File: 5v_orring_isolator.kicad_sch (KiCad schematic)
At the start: 11 parts, among them IC2 NPS4053GVH, U4 TBA2-2411, U6 TPS2116DRL

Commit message: footprint assignment again
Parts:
- C20: renamed from C19; footprint (none) -> Capacitor_SMD:C_0805_2012Metric
- C21: footprint (none) -> Capacitor_SMD:C_0805_2012Metric
- C22: renamed from C20; footprint (none) -> Capacitor_SMD:C_0805_2012Metric
- IC2: footprint SOT95P275X110-6N -> UTSVT_Power:SOT95P275X110-6N
- R36, R37: footprint (none) -> Resistor_SMD:R_0805_2012Metric
- renumbered R28 to R33, R29 to R34, R30 to R35, U6 to U5, U4 to U6
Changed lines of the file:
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@@
 		(dnp no)
 		(fields_autoplaced yes)
-		(property "Reference" "#PWR050"
+		(property "Reference" "#PWR060"
 			(at 39.37 121.92 0)
 			(effects
@@
 			(project "USBCPowerPCB"
 				(path "/f58400c5-df4b-4929-8d2b-33c0fe23fcd9/3390d9c6-6b88-417e-a6aa-b25c6fe8fa66"
-					(reference "#PWR050")
+					(reference "#PWR060")
 					(unit 1)
 				)
@@
 		(dnp no)
 		(fields_autoplaced yes)
-		(property "Reference" "U4"
+		(property "Reference" "U6"
 			(at 147.32 95.25 0)
 			(effects
@@
 			(project ""
 				(path "/f58400c5-df4b-4929-8d2b-33c0fe23fcd9/3390d9c6-6b88-417e-a6aa-b25c6fe8fa66"
-					(reference "U4")
+					(reference "U6")
 					(unit 1)
 				)
@@
 		(dnp no)
 		(fields_autoplaced yes)
-		(property "Reference" "#PWR035"
+		(property "Reference" "#PWR061"
 			(at 85.09 121.92 0)
 			(effects
@@
 			(project "USBCPowerPCB"
 				(path "/f58400c5-df4b-4929-8d2b-33c0fe23fcd9/3390d9c6-6b88-417e-a6aa-b25c6fe8fa66"
-					(reference "#PWR035")
+					(reference "#PWR061")
 					(unit 1)
 				)
@@
 		(on_board yes)
 		(dnp no)
-		(property "Reference" "#PWR067"
+		(property "Reference" "#PWR064"
 			(at 194.31 111.76 0)
 			(effects
@@
 			(project "USBCPowerPCB"
 				(path "/f58400c5-df4b-4929-8d2b-33c0fe23fcd9/3390d9c6-6b88-417e-a6aa-b25c6fe8fa66"
-					(reference "#PWR067")
+					(reference "#PWR064")
 					(unit 1)
 				)
@@
 		(dnp no)
 		(fields_autoplaced yes)
-		(property "Reference" "R28"
+		(property "Reference" "R33"
 			(at 41.91 99.0599 0)
 			(effects
@@
 			(project "USBCPowerPCB"
 				(path "/f58400c5-df4b-4929-8d2b-33c0fe23fcd9/3390d9c6-6b88-417e-a6aa-b25c6fe8fa66"
-					(reference "R28")
+					(reference "R33")
 					(unit 1)
 				)
@@
 		(on_board yes)
 		(dnp no)
-		(property "Reference" "#PWR043"
+		(property "Reference" "#PWR063"
 			(at 158.75 114.3 0)
 			(effects
@@
 			(project "USBCPowerPCB"
 				(path "/f58400c5-df4b-4929-8d2b-33c0fe23fcd9/3390d9c6-6b88-417e-a6aa-b25c6fe8fa66"
-					(reference "#PWR043")
+					(reference "#PWR063")
 					(unit 1)
 				)
@@
 		(on_board yes)
 		(dnp no)
-		(property "Reference" "#PWR042"
+		(property "Reference" "#PWR062"
 			(at 135.89 115.57 0)
 			(effects
@@
 			(project "USBCPowerPCB"
 				(path "/f58400c5-df4b-4929-8d2b-33c0fe23fcd9/3390d9c6-6b88-417e-a6aa-b25c6fe8fa66"
-					(reference "#PWR042")
+					(reference "#PWR062")
 					(unit 1)
 				)
@@
 		(dnp no)
 		(fields_autoplaced yes)
-		(property "Reference" "U6"
+		(property "Reference" "U5"
 			(at 85.09 91.44 0)
 			(effects
@@
 			(project "USBCPowerPCB"
 				(path "/f58400c5-df4b-4929-8d2b-33c0fe23fcd9/3390d9c6-6b88-417e-a6aa-b25c6fe8fa66"
-					(reference "U6")
+					(reference "U5")
 					(unit 1)
 				)
@@
 		(dnp no)
 		(fields_autoplaced yes)
-		(property "Reference" "R30"
+		(property "Reference" "R35"
 			(at 99.06 102.8699 0)
 			(effects
@@
 			(project "USBCPowerPCB"
 				(path "/f58400c5-df4b-4929-8d2b-33c0fe23fcd9/3390d9c6-6b88-417e-a6aa-b25c6fe8fa66"
-					(reference "R30")
+					(reference "R35")
 					(unit 1)
 				)
@@
 		(dnp no)
 		(fields_autoplaced yes)
-		(property "Reference" "R29"
+		(property "Reference" "R34"
 			(at 41.91 109.2199 0)
 			(effects
@@
 			(project "USBCPowerPCB"
 				(path "/f58400c5-df4b-4929-8d2b-33c0fe23fcd9/3390d9c6-6b88-417e-a6aa-b25c6fe8fa66"
-					(reference "R29")
+					(reference "R34")
 					(unit 1)
 				)
@@
 		(dnp no)
 		(fields_autoplaced yes)
-		(property "Reference" "#PWR065"
+		(property "Reference" "#PWR068"
 			(at 266.7 111.76 0)
 			(effects
@@
 			(project "USBCPowerPCB"
 				(path "/f58400c5-df4b-4929-8d2b-33c0fe23fcd9/3390d9c6-6b88-417e-a6aa-b25c6fe8fa66"
-					(reference "#PWR065")
+					(reference "#PWR068")
 					(unit 1)
 				)
@@
 		(dnp no)
 		(fields_autoplaced yes)
-		(property "Reference" "#PWR068"
+		(property "Reference" "#PWR067"
 			(at 259.08 115.57 0)
 			(effects
@@
 			(project "USBCPowerPCB"
 				(path "/f58400c5-df4b-4929-8d2b-33c0fe23fcd9/3390d9c6-6b88-417e-a6aa-b25c6fe8fa66"
-					(reference "#PWR068")
+					(reference "#PWR067")
 					(unit 1)
 				)
@@
 		(on_board yes)
 		(dnp no)
-		(property "Reference" "C19"
+		(property "Reference" "C20"
 			(at 191.77 101.6062 0)
 			(effects
@@
 			)
 		)
-		(property "Footprint" ""
+		(property "Footprint" "Capacitor_SMD:C_0805_2012Metric"
 			(at 194.31 102.87 0)
 			(effects
@@
 			(project ""
 				(path "/f58400c5-df4b-4929-8d2b-33c0fe23fcd9/3390d9c6-6b88-417e-a6aa-b25c6fe8fa66"
-					(reference "C19")
+					(reference "C20")
 					(unit 1)
 				)
@@
 		(on_board yes)
 		(dnp no)
-		(property "Reference" "#PWR061"
+		(property "Reference" "#PWR066"
 			(at 214.63 107.95 0)
 			(effects
@@
 			(project ""
 				(path "/f58400c5-df4b-4929-8d2b-33c0fe23fcd9/3390d9c6-6b88-417e-a6aa-b25c6fe8fa66"
-					(reference "#PWR061")
+					(reference "#PWR066")
 					(unit 1)
 				)
@@
 			)
 		)
-		(property "Footprint" "SOT95P275X110-6N"
+		(property "Footprint" "UTSVT_Power:SOT95P275X110-6N"
 			(at 243.84 193.98 0)
 			(effects
@@
 		(on_board yes)
 		(dnp no)
-		(property "Reference" "C20"
+		(property "Reference" "C22"
 			(at 269.24 101.6062 0)
 			(effects
@@
 			)
 		)
-		(property "Footprint" ""
+		(property "Footprint" "Capacitor_SMD:C_0805_2012Metric"
 			(at 266.7 102.87 0)
 			(effects
@@
 			(project "USBCPowerPCB"
 				(path "/f58400c5-df4b-4929-8d2b-33c0fe23fcd9/3390d9c6-6b88-417e-a6aa-b25c6fe8fa66"
-					(reference "C20")
+					(reference "C22")
 					(unit 1)
 				)
@@
 			)
 		)
-		(property "Footprint" ""
+		(property "Footprint" "Resistor_SMD:R_0805_2012Metric"
 			(at 204.47 102.87 0)
 			(effects
@@
 		(on_board yes)
 		(dnp no)
-		(property "Reference" "#PWR066"
+		(property "Reference" "#PWR065"
 			(at 204.47 120.65 0)
 			(effects
@@
 			(project "USBCPowerPCB"
 				(path "/f58400c5-df4b-4929-8d2b-33c0fe23fcd9/3390d9c6-6b88-417e-a6aa-b25c6fe8fa66"
-					(reference "#PWR066")
+					(reference "#PWR065")
 					(unit 1)
 				)
@@
 			)
 		)
-		(property "Footprint" ""
+		(property "Footprint" "Capacitor_SMD:C_0805_2012Metric"
 			(at 204.47 111.76 0)
 			(effects
@@
 			)
 		)
-		(property "Footprint" ""
+		(property "Footprint" "Resistor_SMD:R_0805_2012Metric"
 			(at 259.08 106.68 0)
 			(effects

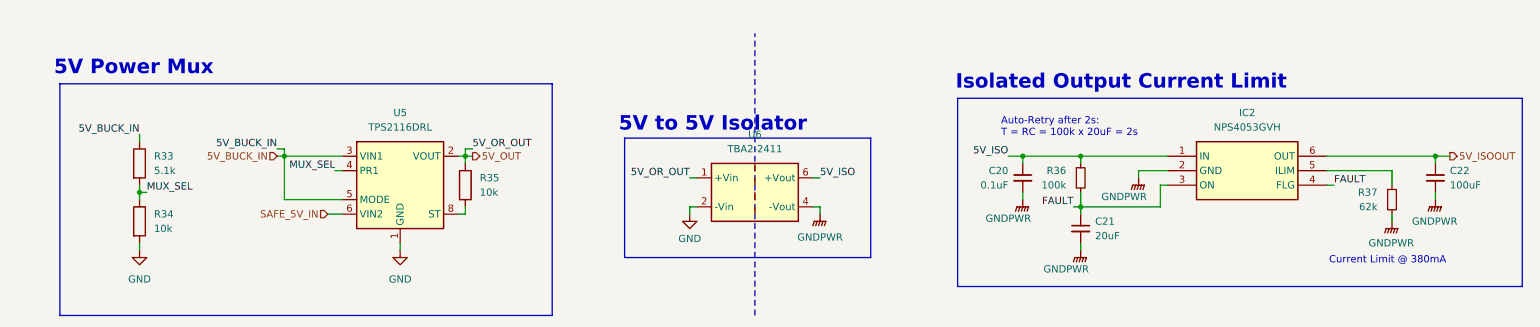
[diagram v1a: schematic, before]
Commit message: finished addressing review comments & organized bom with p/ns for everything
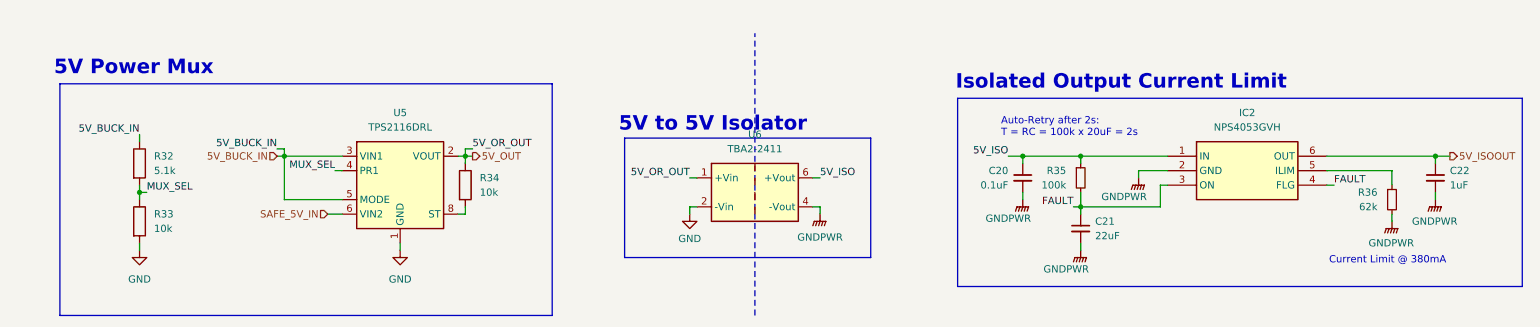
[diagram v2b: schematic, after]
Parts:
- C20: Manufacturer_Name (none) -> KEMET; Mouser Part Number (none) -> C0805C104M5RACTU; Vdc (none) -> 50V
- C21: value 20uF -> 22uF; Manufacturer_Name (none) -> TDK; Mouser Part Number (none) -> C2012X5R1V226M125AC; Vdc (none) -> 35V
- C22: value 100uF -> 1uF; Manufacturer_Name (none) -> KEMET; Mouser Part Number (none) -> C0805C105K5PACTU; Vdc (none) -> 50V
- IC2: Mouser Part Number (none) -> 771-NPS4053GVH
- R32: renamed from R33; Manufacturer_Name (none) -> VISHAY; Mouser Part Number (none) -> CRCW08055K10FKEAC
- R33: renamed from R34; Manufacturer_Name (none) -> VISHAY; Mouser Part Number (none) -> CRCW080510K0FKEAC
- R34: renamed from R35; Manufacturer_Name (none) -> VISHAY; Mouser Part Number (none) -> CRCW080510K0FKEAC
- R35: renamed from R36; Manufacturer_Name (none) -> VISHAY; Mouser Part Number (none) -> CRCW0805100KFKEAC
- R36: renamed from R37; Manufacturer_Name (none) -> VISHAY; Mouser Part Number (none) -> CRCW080562K0FKEAC
- U5: Manufacturer_Name (none) -> Texas Instruments; Mouser Part Number (none) -> 595-TPS2116DRLR
- U6: Manufacturer_Name (none) -> TRACO Power; Mouser Part Number (none) -> 495-TBA2-2411
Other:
- title: (none) -> 5V ORring and Isolator

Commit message: intermediate progress push before addressing Champers' and Lakshay's review comments
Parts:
- renumbered C20 to C21, C21 to C22, C22 to C23
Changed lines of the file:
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@@
 		(dnp no)
 		(fields_autoplaced yes)
-		(property "Reference" "#PWR067"
+		(property "Reference" "#PWR066"
 			(at 39.37 121.92 0)
 			(effects
@@
 			(project "USBCPowerPCB"
 				(path "/f58400c5-df4b-4929-8d2b-33c0fe23fcd9/3390d9c6-6b88-417e-a6aa-b25c6fe8fa66"
-					(reference "#PWR067")
+					(reference "#PWR066")
 					(unit 1)
 				)
@@
 		(dnp no)
 		(fields_autoplaced yes)
-		(property "Reference" "#PWR068"
+		(property "Reference" "#PWR067"
 			(at 85.09 121.92 0)
 			(effects
@@
 			(project "USBCPowerPCB"
 				(path "/f58400c5-df4b-4929-8d2b-33c0fe23fcd9/3390d9c6-6b88-417e-a6aa-b25c6fe8fa66"
-					(reference "#PWR068")
+					(reference "#PWR067")
 					(unit 1)
 				)
@@
 		(on_board yes)
 		(dnp no)
-		(property "Reference" "#PWR071"
+		(property "Reference" "#PWR070"
 			(at 194.31 111.76 0)
 			(effects
@@
 			(project "USBCPowerPCB"
 				(path "/f58400c5-df4b-4929-8d2b-33c0fe23fcd9/3390d9c6-6b88-417e-a6aa-b25c6fe8fa66"
-					(reference "#PWR071")
+					(reference "#PWR070")
 					(unit 1)
 				)
@@
 		(on_board yes)
 		(dnp no)
-		(property "Reference" "#PWR070"
+		(property "Reference" "#PWR069"
 			(at 158.75 114.3 0)
 			(effects
@@
 			(project "USBCPowerPCB"
 				(path "/f58400c5-df4b-4929-8d2b-33c0fe23fcd9/3390d9c6-6b88-417e-a6aa-b25c6fe8fa66"
-					(reference "#PWR070")
+					(reference "#PWR069")
 					(unit 1)
 				)
@@
 		(on_board yes)
 		(dnp no)
-		(property "Reference" "#PWR069"
+		(property "Reference" "#PWR068"
 			(at 135.89 115.57 0)
 			(effects
@@
 			(project "USBCPowerPCB"
 				(path "/f58400c5-df4b-4929-8d2b-33c0fe23fcd9/3390d9c6-6b88-417e-a6aa-b25c6fe8fa66"
-					(reference "#PWR069")
+					(reference "#PWR068")
 					(unit 1)
 				)
@@
 		(dnp no)
 		(fields_autoplaced yes)
-		(property "Reference" "#PWR075"
+		(property "Reference" "#PWR074"
 			(at 266.7 111.76 0)
 			(effects
@@
 			(project "USBCPowerPCB"
 				(path "/f58400c5-df4b-4929-8d2b-33c0fe23fcd9/3390d9c6-6b88-417e-a6aa-b25c6fe8fa66"
-					(reference "#PWR075")
+					(reference "#PWR074")
 					(unit 1)
 				)
@@
 		(dnp no)
 		(fields_autoplaced yes)
-		(property "Reference" "#PWR074"
+		(property "Reference" "#PWR073"
 			(at 259.08 115.57 0)
 			(effects
@@
 			(project "USBCPowerPCB"
 				(path "/f58400c5-df4b-4929-8d2b-33c0fe23fcd9/3390d9c6-6b88-417e-a6aa-b25c6fe8fa66"
-					(reference "#PWR074")
+					(reference "#PWR073")
 					(unit 1)
 				)
@@
 		(on_board yes)
 		(dnp no)
-		(property "Reference" "C20"
+		(property "Reference" "C21"
 			(at 191.77 101.6062 0)
 			(effects
@@
 			(project ""
 				(path "/f58400c5-df4b-4929-8d2b-33c0fe23fcd9/3390d9c6-6b88-417e-a6aa-b25c6fe8fa66"
-					(reference "C20")
+					(reference "C21")
 					(unit 1)
 				)
@@
 		(on_board yes)
 		(dnp no)
-		(property "Reference" "#PWR073"
+		(property "Reference" "#PWR072"
 			(at 214.63 107.95 0)
 			(effects
@@
 			(project ""
 				(path "/f58400c5-df4b-4929-8d2b-33c0fe23fcd9/3390d9c6-6b88-417e-a6aa-b25c6fe8fa66"
-					(reference "#PWR073")
+					(reference "#PWR072")
 					(unit 1)
 				)
@@
 		(on_board yes)
 		(dnp no)
-		(property "Reference" "C22"
+		(property "Reference" "C23"
 			(at 269.24 101.6062 0)
 			(effects
@@
 			(project "USBCPowerPCB"
 				(path "/f58400c5-df4b-4929-8d2b-33c0fe23fcd9/3390d9c6-6b88-417e-a6aa-b25c6fe8fa66"
-					(reference "C22")
+					(reference "C23")
 					(unit 1)
 				)
@@
 		(on_board yes)
 		(dnp no)
-		(property "Reference" "#PWR072"
+		(property "Reference" "#PWR071"
 			(at 204.47 120.65 0)
 			(effects
@@
 			(project "USBCPowerPCB"
 				(path "/f58400c5-df4b-4929-8d2b-33c0fe23fcd9/3390d9c6-6b88-417e-a6aa-b25c6fe8fa66"
-					(reference "#PWR072")
+					(reference "#PWR071")
 					(unit 1)
 				)
@@
 		(on_board yes)
 		(dnp no)
-		(property "Reference" "C21"
+		(property "Reference" "C22"
 			(at 207.01 110.4962 0)
 			(effects
@@
 			(project "USBCPowerPCB"
 				(path "/f58400c5-df4b-4929-8d2b-33c0fe23fcd9/3390d9c6-6b88-417e-a6aa-b25c6fe8fa66"
-					(reference "C21")
-					(unit 1)
-				)
+					(reference "C22")
+					(unit 1)
+				)

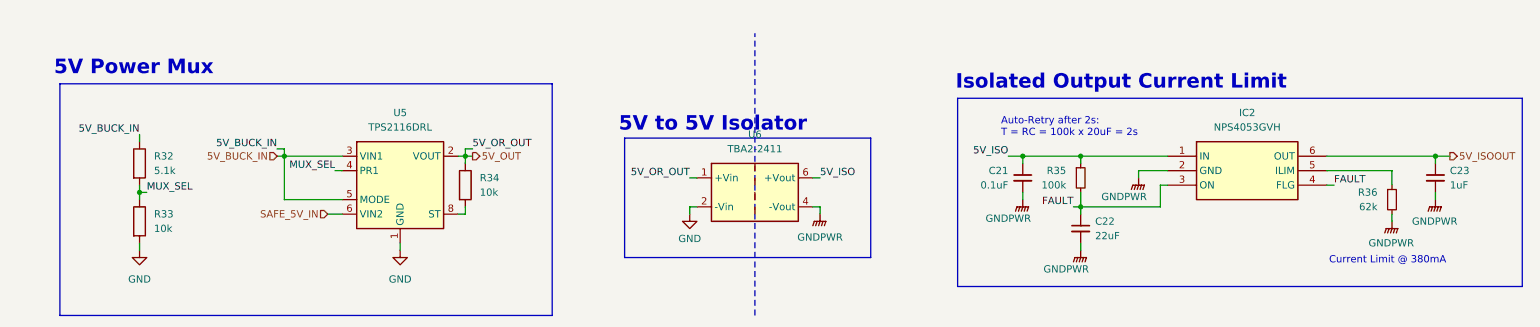
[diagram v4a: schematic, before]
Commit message: Addressed most of the review comments, fixed power protection, added bigger caps & better part selection on 12V and 5V out, changed 5V buck inductor, fixed power good & fault LEDs
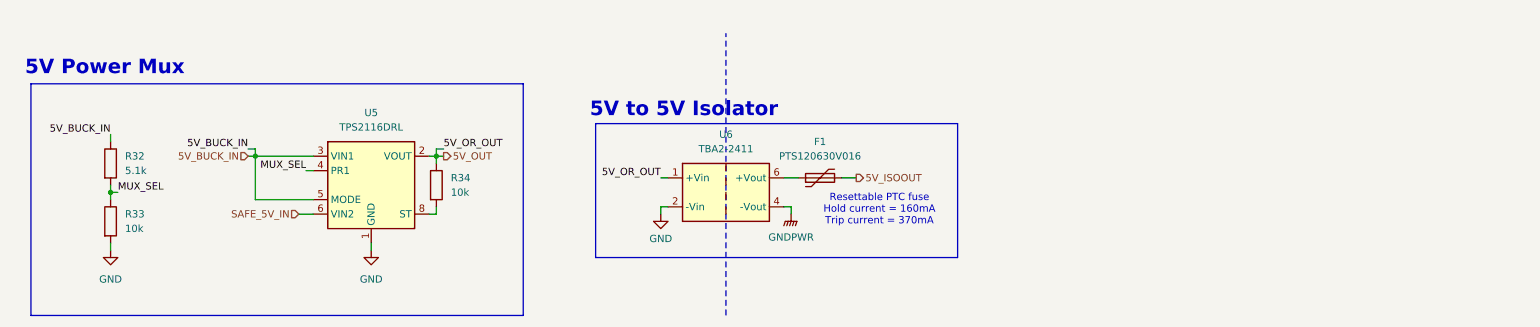
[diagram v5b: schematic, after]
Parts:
- removed C21: 0.1uF, Capacitor_SMD:C_0805_2012Metric, symbol Device:C_Small
- removed C22: 22uF, Capacitor_SMD:C_0805_2012Metric, symbol Device:C_Small
- removed C23: 1uF, Capacitor_SMD:C_0805_2012Metric, symbol Device:C_Small
- removed IC2: NPS4053GVH, UTSVT_Power:SOT95P275X110-6N, symbol utsvt-chips:NPS4053GVH
- removed R35: 100k, Resistor_SMD:R_0805_2012Metric, symbol Device:R_Small
- removed R36: 62k, Resistor_SMD:R_0805_2012Metric, symbol Device:R_Small
- added F1: PTS120630V016, symbol Device:Polyfuse
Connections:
- net 5V_ISOOUT: now also F1.2
- net 5V_ISO: no longer names the net of U6.6 (+Vout)
- net 5V_ISO: now also F1.1
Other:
- note added: "Resettable PTC fuse Hold current = 160mA Trip current = 370mA"
- note removed: "Auto-Retry after 2s: T = RC = 100k x 20uF = 2s"
- note removed: "Current Limit @ 380mA"
- note removed: "Isolated Output Current Limit"
- moved on the sheet: R32, R33, R34, U5, U6

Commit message: Added ideal diode controller & mosfet for 12V buck power protection
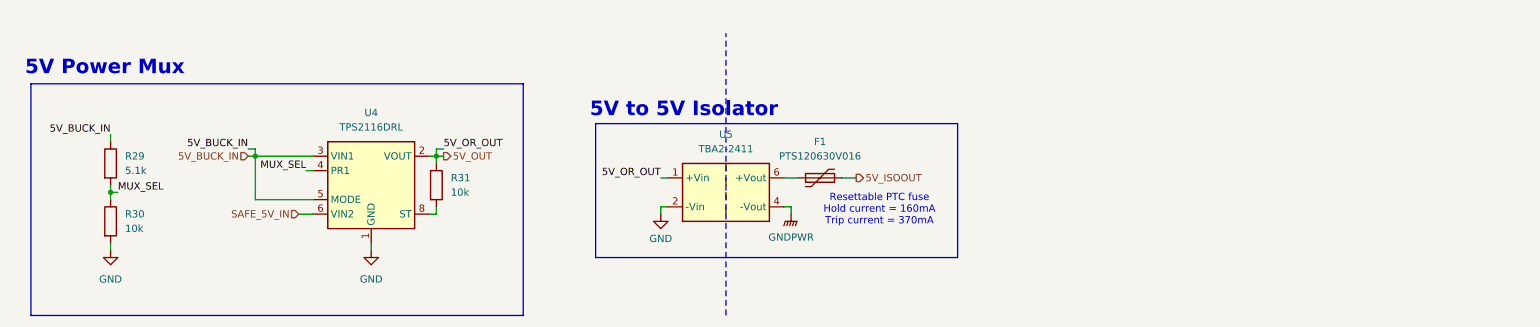
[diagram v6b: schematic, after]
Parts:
- F1: footprint (none) -> Fuse:Fuse_1206_3216Metric; Manufacturer_Name (none) -> Eaton; Mouser Part Number (none) -> PTS120630V016
- renumbered R32 to R29, R33 to R30, R34 to R31, U5 to U4, U6 to U5
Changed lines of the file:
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@@
 		(dnp no)
 		(fields_autoplaced yes)
-		(property "Reference" "#PWR066"
+		(property "Reference" "#PWR063"
 			(at 34.29 121.92 0)
 			(effects
@@
 			(project "USBCPowerPCB"
 				(path "/f58400c5-df4b-4929-8d2b-33c0fe23fcd9/3390d9c6-6b88-417e-a6aa-b25c6fe8fa66"
-					(reference "#PWR066")
+					(reference "#PWR063")
 					(unit 1)
 				)
@@
 		(dnp no)
 		(fields_autoplaced yes)
-		(property "Reference" "U6"
+		(property "Reference" "U5"
 			(at 142.24 95.25 0)
 			(effects
@@
 			(project ""
 				(path "/f58400c5-df4b-4929-8d2b-33c0fe23fcd9/3390d9c6-6b88-417e-a6aa-b25c6fe8fa66"
-					(reference "U6")
+					(reference "U5")
 					(unit 1)
 				)
@@
 		(dnp no)
 		(fields_autoplaced yes)
-		(property "Reference" "#PWR067"
+		(property "Reference" "#PWR064"
 			(at 80.01 121.92 0)
 			(effects
@@
 			(project "USBCPowerPCB"
 				(path "/f58400c5-df4b-4929-8d2b-33c0fe23fcd9/3390d9c6-6b88-417e-a6aa-b25c6fe8fa66"
-					(reference "#PWR067")
+					(reference "#PWR064")
 					(unit 1)
 				)
@@
 		(dnp no)
 		(fields_autoplaced yes)
-		(property "Reference" "R32"
+		(property "Reference" "R29"
 			(at 36.83 99.0599 0)
 			(effects
@@
 			(project "USBCPowerPCB"
 				(path "/f58400c5-df4b-4929-8d2b-33c0fe23fcd9/3390d9c6-6b88-417e-a6aa-b25c6fe8fa66"
-					(reference "R32")
+					(reference "R29")
 					(unit 1)
 				)
@@
 		(on_board yes)
 		(dnp no)
-		(property "Reference" "#PWR069"
+		(property "Reference" "#PWR066"
 			(at 153.67 114.3 0)
 			(effects
@@
 			(project "USBCPowerPCB"
 				(path "/f58400c5-df4b-4929-8d2b-33c0fe23fcd9/3390d9c6-6b88-417e-a6aa-b25c6fe8fa66"
-					(reference "#PWR069")
+					(reference "#PWR066")
 					(unit 1)
 				)
@@
 			)
 		)
-		(property "Footprint" ""
+		(property "Footprint" "Fuse:Fuse_1206_3216Metric"
 			(at 163.83 101.6 0)
 			(effects
@@
 		)
 		(property "SnapEDA_Link" ""
+			(at 158.75 102.87 0)
+			(effects
+				(font
+					(size 1.27 1.27)
+				)
+				(hide yes)
+			)
+		)
+		(property "Manufacturer_Name" "Eaton"
+			(at 158.75 102.87 0)
+			(effects
+				(font
+					(size 1.27 1.27)
+				)
+				(hide yes)
+			)
+		)
+		(property "Mouser Part Number" "PTS120630V016"
 			(at 158.75 102.87 0)
 			(effects
@@
 		(on_board yes)
 		(dnp no)
-		(property "Reference" "#PWR068"
+		(property "Reference" "#PWR065"
 			(at 130.81 115.57 0)
 			(effects
@@
 			(project "USBCPowerPCB"
 				(path "/f58400c5-df4b-4929-8d2b-33c0fe23fcd9/3390d9c6-6b88-417e-a6aa-b25c6fe8fa66"
-					(reference "#PWR068")
+					(reference "#PWR065")
 					(unit 1)
 				)
@@
 		(dnp no)
 		(fields_autoplaced yes)
-		(property "Reference" "U5"
+		(property "Reference" "U4"
 			(at 80.01 91.44 0)
 			(effects
@@
 			(project "USBCPowerPCB"
 				(path "/f58400c5-df4b-4929-8d2b-33c0fe23fcd9/3390d9c6-6b88-417e-a6aa-b25c6fe8fa66"
-					(reference "U5")
+					(reference "U4")
 					(unit 1)
 				)
@@
 		(dnp no)
 		(fields_autoplaced yes)
-		(property "Reference" "R34"
+		(property "Reference" "R31"
 			(at 93.98 102.8699 0)
 			(effects
@@
 			(project "USBCPowerPCB"
 				(path "/f58400c5-df4b-4929-8d2b-33c0fe23fcd9/3390d9c6-6b88-417e-a6aa-b25c6fe8fa66"
-					(reference "R34")
+					(reference "R31")
 					(unit 1)
 				)
@@
 		(dnp no)
 		(fields_autoplaced yes)
-		(property "Reference" "R33"
+		(property "Reference" "R30"
 			(at 36.83 109.2199 0)
 			(effects
@@
 			(project "USBCPowerPCB"
 				(path "/f58400c5-df4b-4929-8d2b-33c0fe23fcd9/3390d9c6-6b88-417e-a6aa-b25c6fe8fa66"
-					(reference "R33")
+					(reference "R30")
 					(unit 1)
 				)
